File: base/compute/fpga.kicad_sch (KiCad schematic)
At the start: 17 parts, among them U4 W25X20CLSN, U5 ICE40UP5K-SG48ITR-FPGA_Lattice

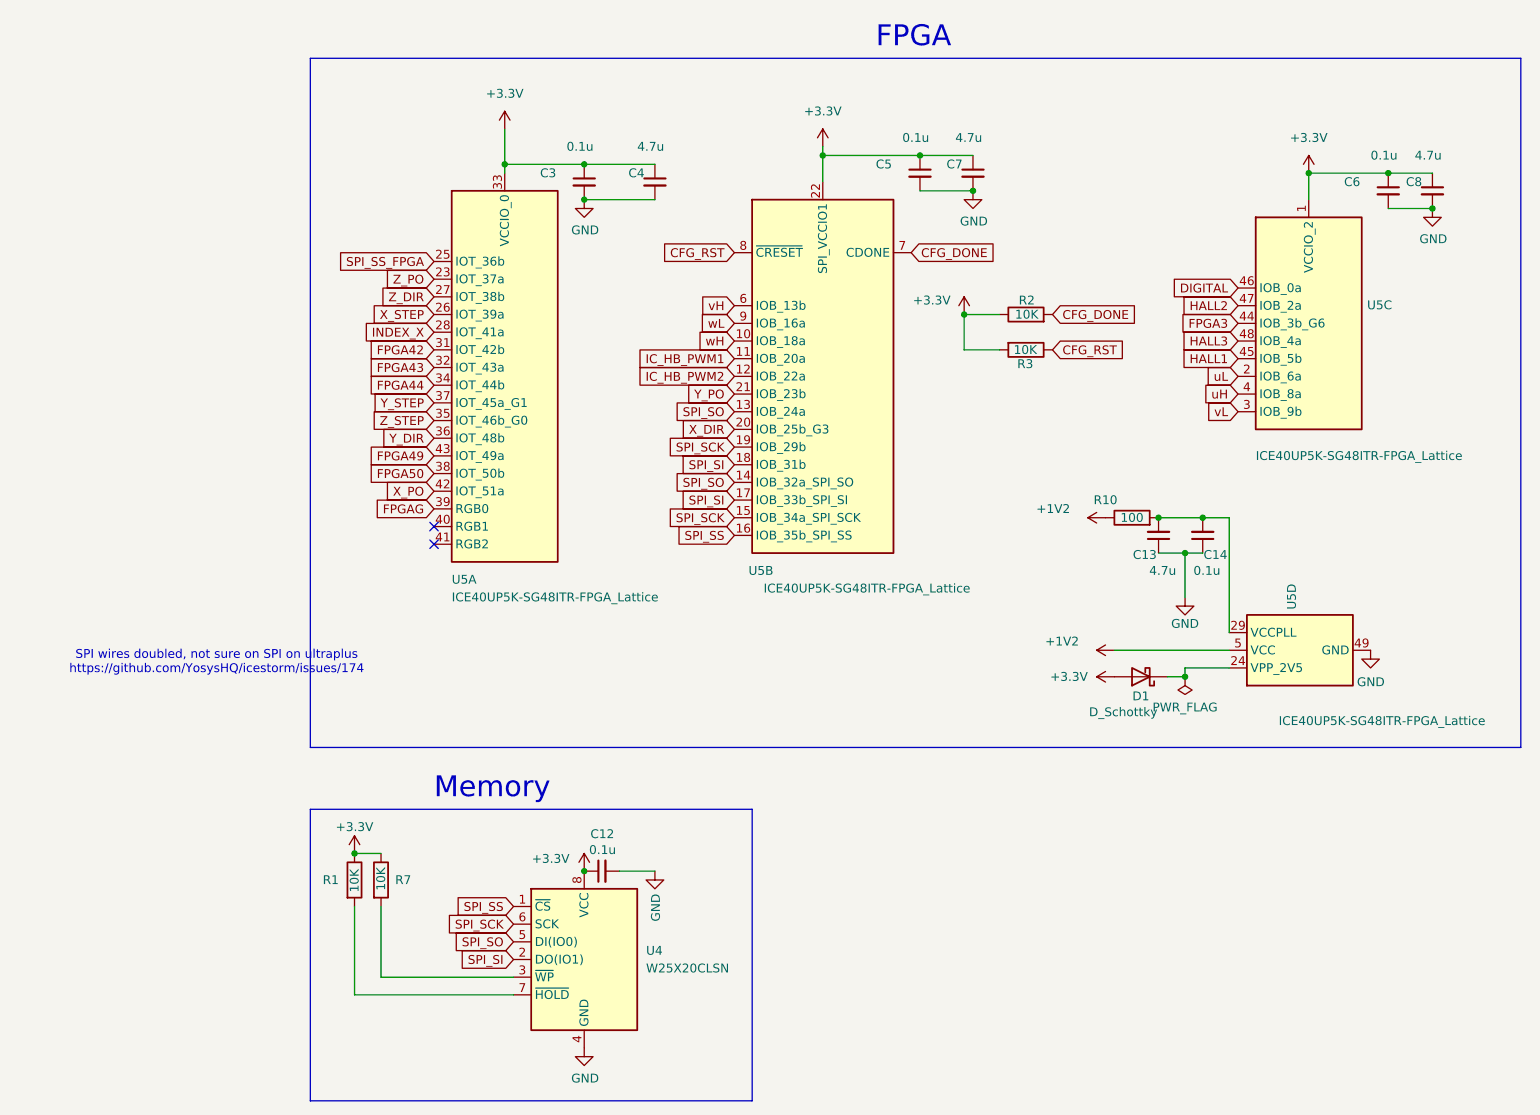
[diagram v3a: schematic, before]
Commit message: compute board 4 layer, with camera connector and small bug fixes
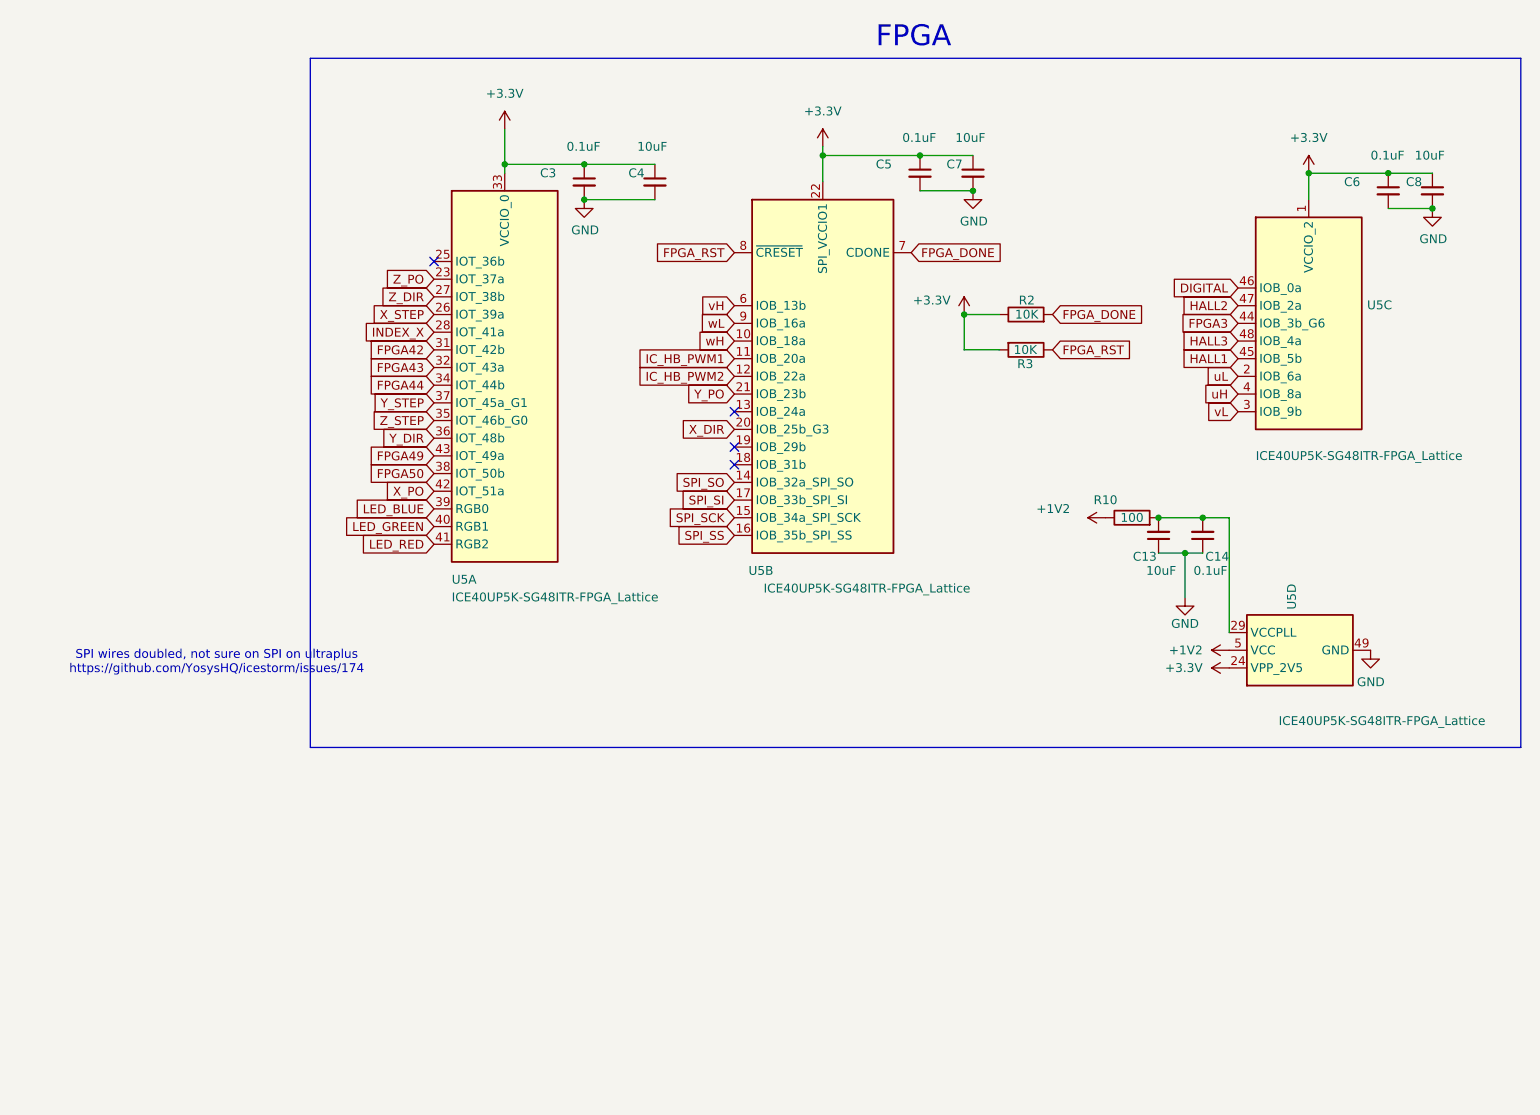
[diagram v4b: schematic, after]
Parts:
- removed C12: 0.1u, Capacitor_SMD:C_0805_2012Metric_Pad1.18x1.45mm_HandSolder, symbol Device:C_Small
- removed D1: D_Schottky, Diode_SMD:D_SOD-323_HandSoldering, symbol Device:D_Schottky
- removed R1, R7: 10K, Resistor_SMD:R_0805_2012Metric, symbol Device:R
- removed U4: W25X20CLSN, Package_SO:SOIC-8_3.9x4.9mm_P1.27mm, symbol Memory_Flash:W25X20CLSN
- C13, C4, C7, C8: value 4.7u -> 10uF; farnell# 2611942 -> 3013485; manf# GRM21BR61H475KE51L -> CL21B106KOQNNNE; mouser# 81-GRM21BR61H475KE1L -> 187-CL21B106KOQNNNE
- C14, C3, C5, C6: value 0.1u -> 0.1uF
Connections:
- net +3.3V: now also U5.24 (VPP_2V5)
- net SPI_SCK: no longer U5.19 (IOB_29b)
- net SPI_SI: no longer U5.18 (IOB_31b)
- net SPI_SO: no longer U5.13 (IOB_24a)
- net LED_GREEN: now reaches U5.40 (RGB1)
- net LED_RED: now reaches U5.41 (RGB2)
- net CFG_DONE renamed FPGA_DONE
- net CFG_RST renamed FPGA_RST
- net FPGAG renamed LED_BLUE
- net SPI_SS_FPGA: no longer names the net of U5.25 (IOT_36b)
- no-connect marks 2 -> 4
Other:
- note removed: "Memory"

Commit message: schema  extension finished, pre  merge
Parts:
- C13, C4, C7, C8: farnell# 3013485 -> 3010126; manf# CL21B106KOQNNNE -> CL21A106KAYNNNE; mouser# 187-CL21B106KOQNNNE -> 187-CL21A106KAYNNNE
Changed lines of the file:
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@@
 			)
 		)
-		(property "manf#" "CL21B106KOQNNNE"
+		(property "manf#" "CL21A106KAYNNNE"
 			(at 105.41 38.1 0)
 			(hide yes)
@@
 			)
 		)
-		(property "farnell#" "3013485"
+		(property "farnell#" "3010126"
 			(at 105.41 38.1 0)
 			(hide yes)
@@
 			)
 		)
-		(property "mouser#" "187-CL21B106KOQNNNE"
+		(property "mouser#" "187-CL21A106KAYNNNE"
 			(at 105.41 38.1 0)
 			(hide yes)
@@
 			)
 		)
-		(property "manf#" "CL21B106KOQNNNE"
+		(property "manf#" "CL21A106KAYNNNE"
 			(at 151.13 36.83 0)
 			(hide yes)
@@
 			)
 		)
-		(property "farnell#" "3013485"
+		(property "farnell#" "3010126"
 			(at 151.13 36.83 0)
 			(hide yes)
@@
 			)
 		)
-		(property "mouser#" "187-CL21B106KOQNNNE"
+		(property "mouser#" "187-CL21A106KAYNNNE"
 			(at 151.13 36.83 0)
 			(hide yes)
@@
 			)
 		)
-		(property "manf#" "CL21B106KOQNNNE"
+		(property "manf#" "CL21A106KAYNNNE"
 			(at 177.8 88.9 0)
 			(hide yes)
@@
 			)
 		)
-		(property "farnell#" "3013485"
+		(property "farnell#" "3010126"
 			(at 177.8 88.9 0)
 			(hide yes)
@@
 			)
 		)
-		(property "mouser#" "187-CL21B106KOQNNNE"
+		(property "mouser#" "187-CL21A106KAYNNNE"
 			(at 177.8 88.9 0)
 			(hide yes)
@@
 			)
 		)
-		(property "manf#" "CL21B106KOQNNNE"
+		(property "manf#" "CL21A106KAYNNNE"
 			(at 217.17 39.37 0)
 			(hide yes)
@@
 			)
 		)
-		(property "farnell#" "3013485"
+		(property "farnell#" "3010126"
 			(at 217.17 39.37 0)
 			(hide yes)
@@
 			)
 		)
-		(property "mouser#" "187-CL21B106KOQNNNE"
+		(property "mouser#" "187-CL21A106KAYNNNE"
 			(at 217.17 39.37 0)
 			(hide yes)

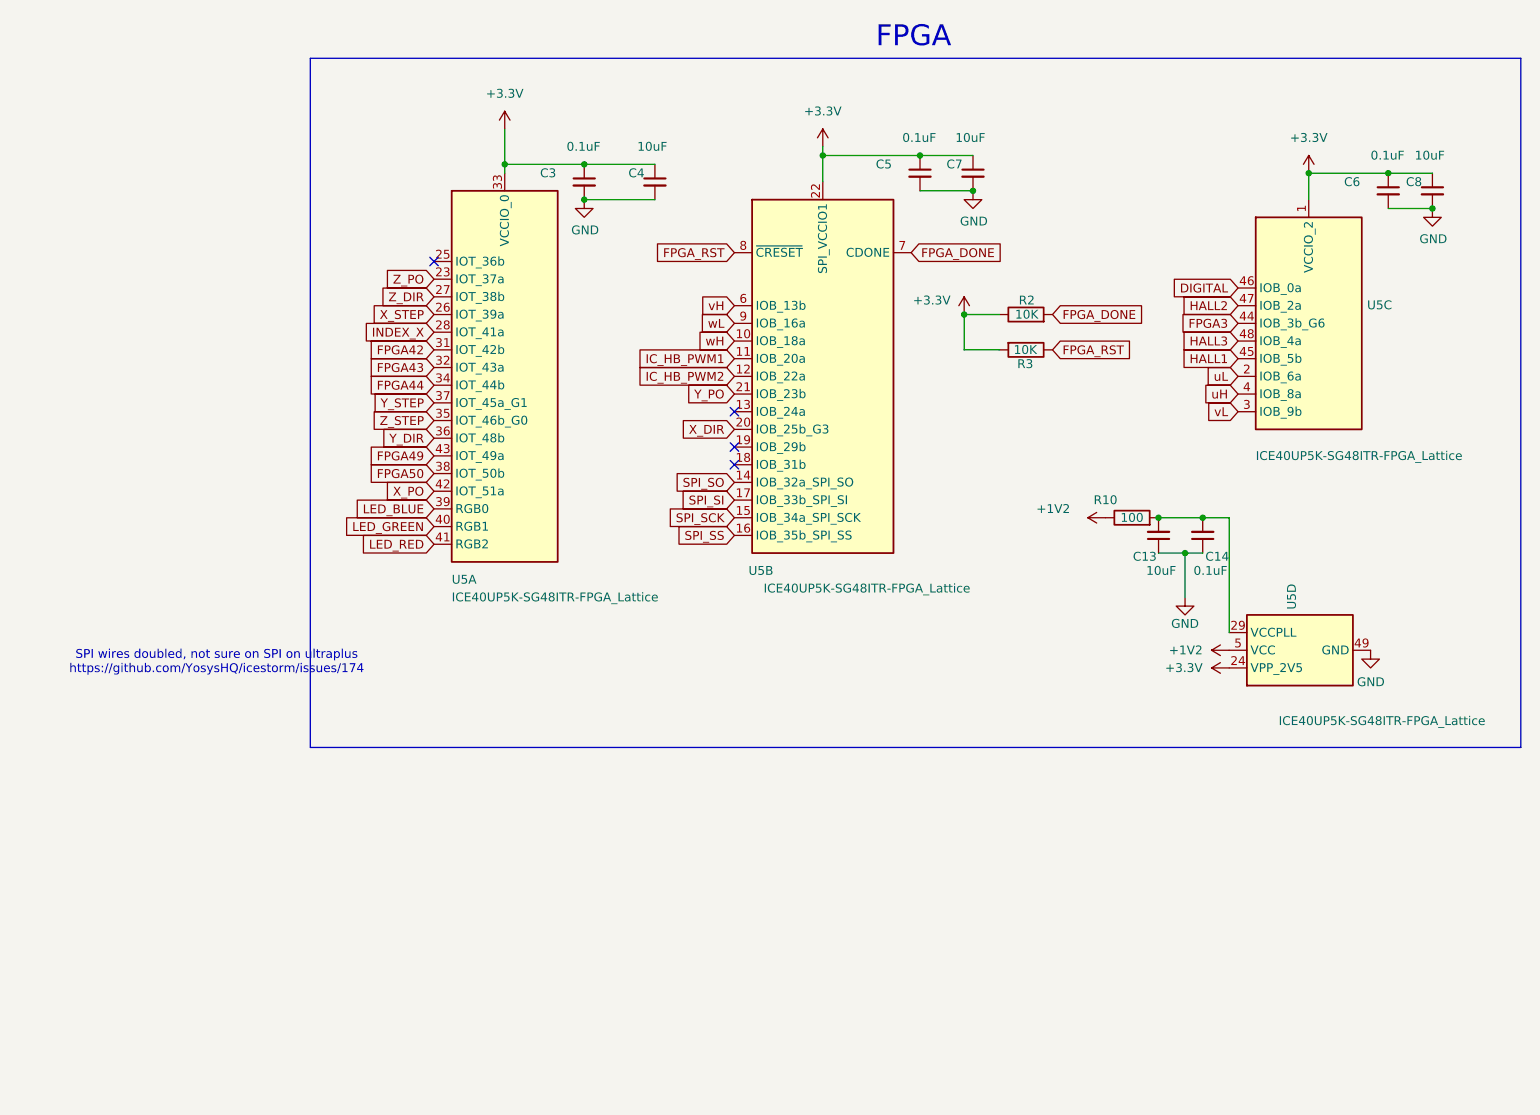
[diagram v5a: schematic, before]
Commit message: quick backup, decided to merge compute and extension
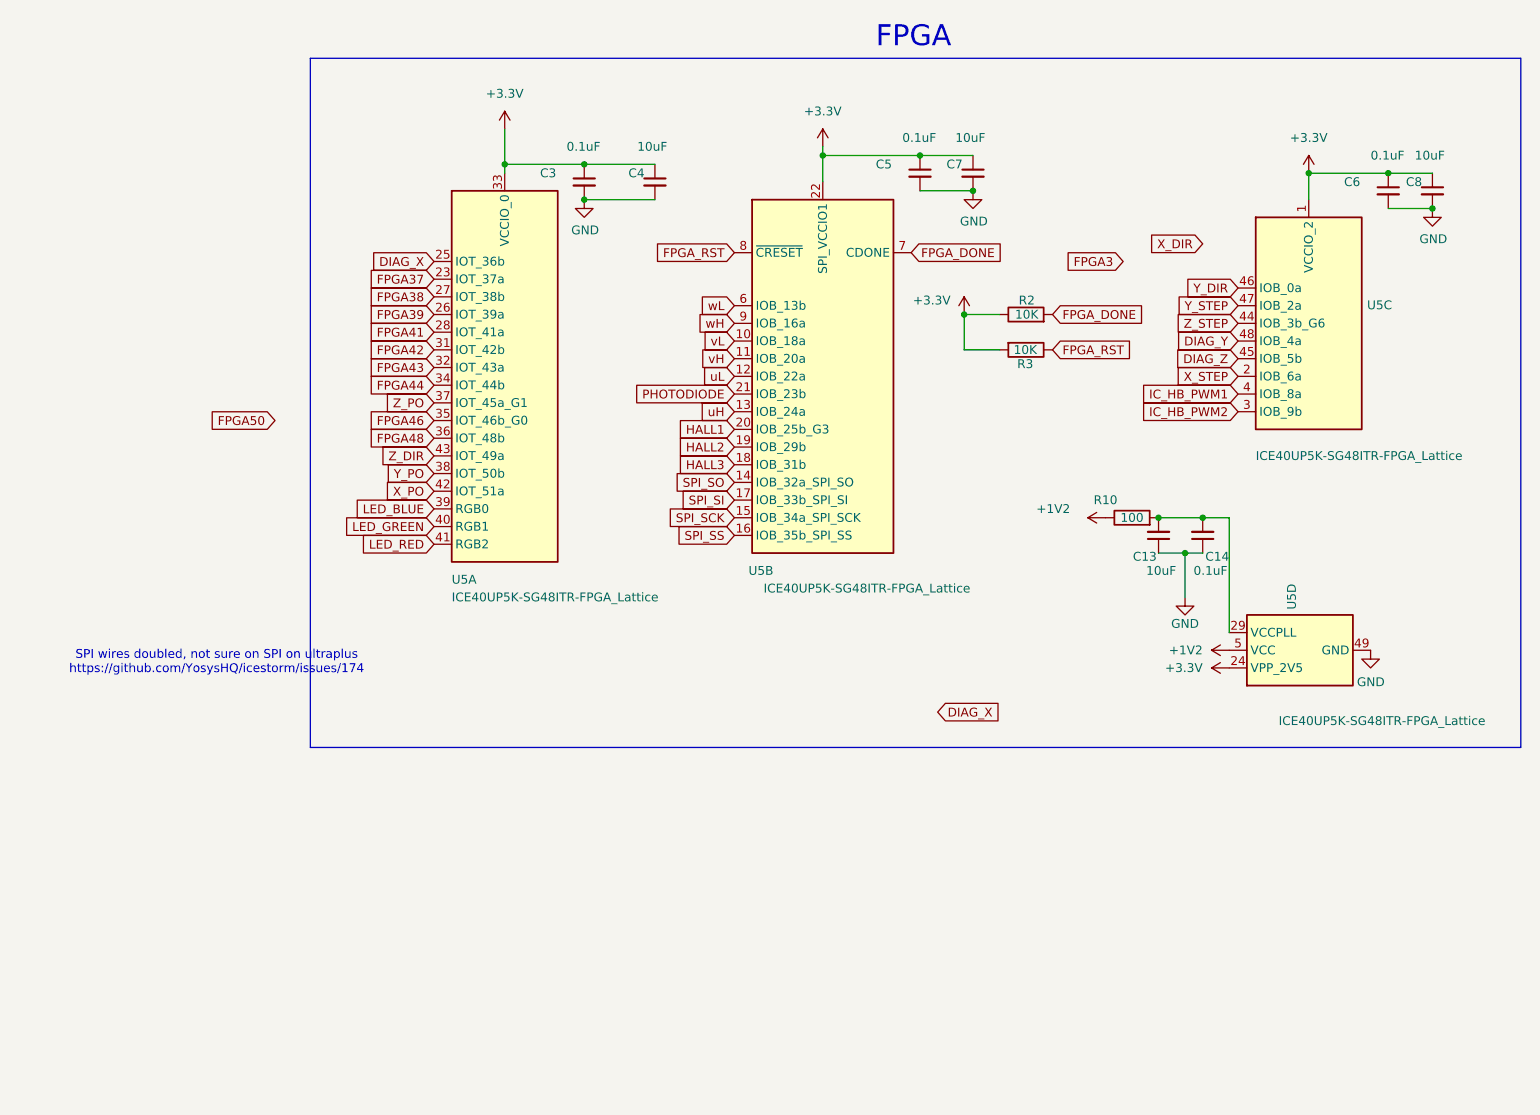
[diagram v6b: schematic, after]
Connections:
- net DIGITAL is gone; now on net Y_DIR: U5.46 (IOB_0a)
- net FPGA49 is gone; now on net Z_DIR: U5.43 (IOT_49a)
- net FPGA3: no longer U5.44 (IOB_3b_G6)
- net FPGA50: no longer U5.38 (IOT_50b)
- net HALL1: now also U5.20 (IOB_25b_G3); no longer U5.45 (IOB_5b)
- net HALL2: now also U5.19 (IOB_29b); no longer U5.47 (IOB_2a)
- net HALL3: now also U5.18 (IOB_31b); no longer U5.48 (IOB_4a)
- net IC_HB_PWM1: now also U5.4 (IOB_8a); no longer U5.11 (IOB_20a)
- net IC_HB_PWM2: now also U5.3 (IOB_9b); no longer U5.12 (IOB_22a)
- net X_DIR: no longer U5.20 (IOB_25b_G3)
- net X_STEP: now also U5.2 (IOB_6a); no longer U5.26 (IOT_39a)
- net Y_DIR: no longer U5.36 (IOT_48b)
- net Y_PO: now also U5.38 (IOT_50b); no longer U5.21 (IOB_23b)
- net Y_STEP: now also U5.47 (IOB_2a); no longer U5.37 (IOT_45a_G1)
- net Z_DIR: no longer U5.27 (IOT_38b)
- net Z_PO: now also U5.37 (IOT_45a_G1); no longer U5.23 (IOT_37a)
- net Z_STEP: now also U5.44 (IOB_3b_G6); no longer U5.35 (IOT_46b_G0)
- net uH: now also U5.13 (IOB_24a); no longer U5.4 (IOB_8a)
- net uL: now also U5.12 (IOB_22a); no longer U5.2 (IOB_6a)
- net vH: now also U5.11 (IOB_20a); no longer U5.6 (IOB_13b)
- net vL: now also U5.10 (IOB_18a); no longer U5.3 (IOB_9b)
- net wH: now also U5.9 (IOB_16a); no longer U5.10 (IOB_18a)
- net wL: now also U5.6 (IOB_13b); no longer U5.9 (IOB_16a)
- net DIAG_X: now reaches U5.25 (IOT_36b)
- net INDEX_X renamed FPGA41
- new net DIAG_Y: U5.48 (IOB_4a)
- new net DIAG_Z: U5.45 (IOB_5b)
- new net FPGA37: U5.23 (IOT_37a)
- new net FPGA38: U5.27 (IOT_38b)
- new net FPGA39: U5.26 (IOT_39a)
- new net FPGA46: U5.35 (IOT_46b_G0)
- new net FPGA48: U5.36 (IOT_48b)
- new net PHOTODIODE: U5.21 (IOB_23b)
- no-connect marks 4 -> 0
